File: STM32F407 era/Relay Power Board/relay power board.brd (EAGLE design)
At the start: 135.9 x 58.4 mm, 37 parts, among them X1 5566-6, X2 22-23-2031, X3 22-23-2021, X4 22-23-2021

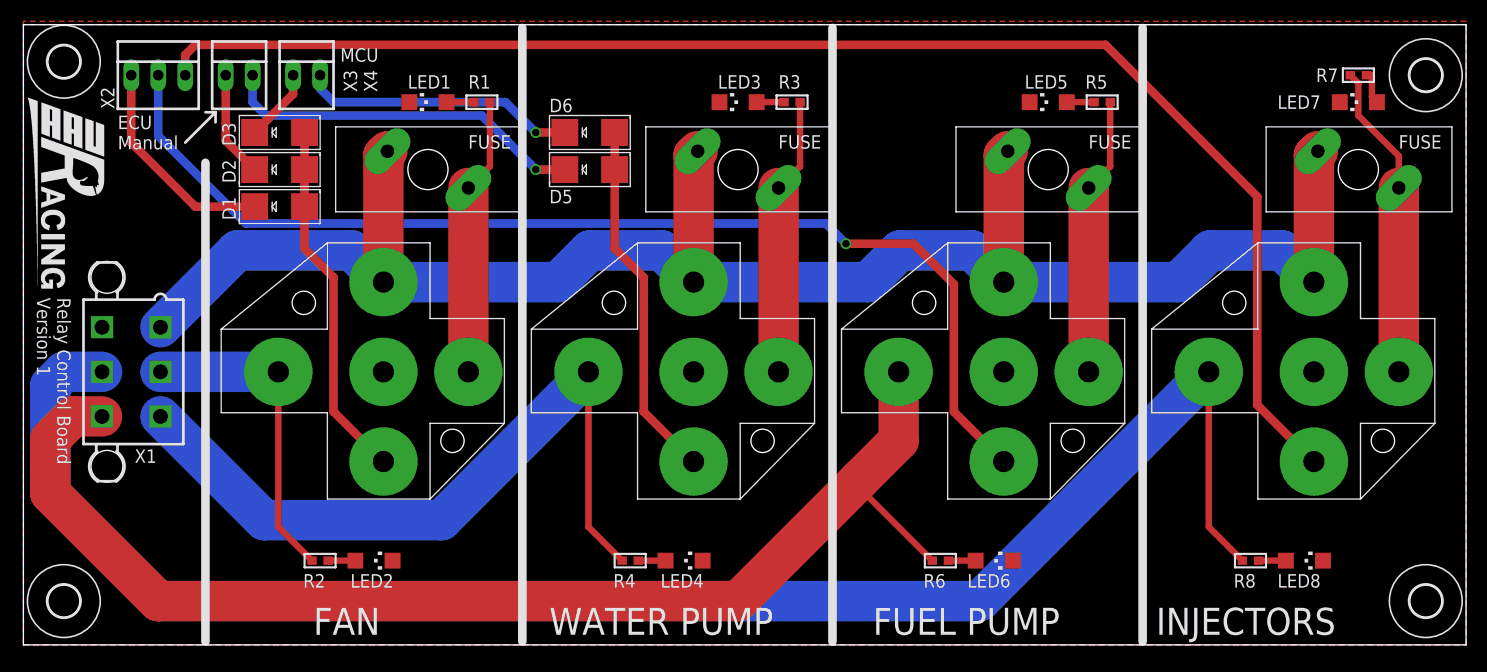
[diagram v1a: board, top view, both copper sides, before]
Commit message: silkscreen changes
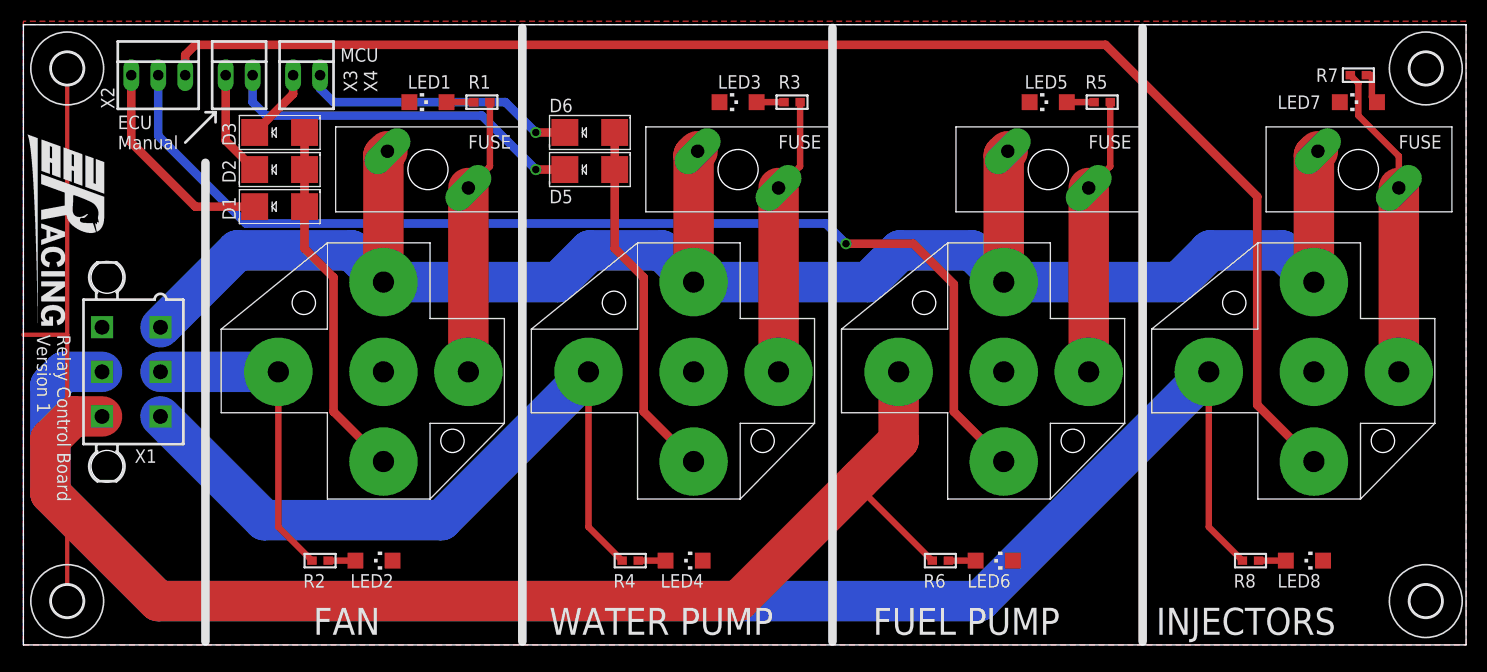
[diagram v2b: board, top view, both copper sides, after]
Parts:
- moved H3 0.71 mm to (4.13, 54.3)
- moved H2 0.63 mm to (132.1, 54.3)
- moved H6 0.32 mm to (4.13, 4.13)
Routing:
- net N$27: track 0.00 -> 54.3 mm

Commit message: All boards RC done!
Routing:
- net N$27: track 54.3 -> 0.00 mm
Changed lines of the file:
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@@
 Version 1</text>
 <wire x1="15.24" y1="47.3075" x2="18.0975" y2="50.165" width="0.254" layer="112"/>
-<dimension x1="0" y1="58.42" x2="0" y2="0" x3="-7.62" y3="29.21" layer="1"/>
-<dimension x1="135.89" y1="58.7375" x2="0" y2="58.7375" x3="67.945" y3="69.5325" layer="1"/>
-<dimension x1="0" y1="0" x2="0" y2="29.21" x3="-7.62" y3="14.605" layer="1"/>
-<dimension x1="4.1275" y1="29.21" x2="4.1275" y2="54.2925" x3="-2.2225" y3="41.75125" layer="1"/>
-<dimension x1="4.1275" y1="4.1275" x2="4.1275" y2="29.21" x3="-2.2225" y3="16.66875" layer="1"/>
-<dimension x1="0" y1="29.21" x2="4.1275" y2="29.21" x3="2.06375" y3="62.865" layer="1"/>
 <wire x1="4.1275" y1="29.21" x2="132.08" y2="29.21" width="0.4064" layer="37"/>
 <wire x1="132.08" y1="29.21" x2="132.08" y2="54.2925" width="0.4064" layer="37"/>
@@
 </signal>
 <signal name="N$27">
-<wire x1="0" y1="29.21" x2="4.1275" y2="29.21" width="0.4064" layer="1"/>
-<wire x1="4.1275" y1="29.21" x2="4.1275" y2="54.2925" width="0.4064" layer="1"/>
-<wire x1="4.1275" y1="4.1275" x2="4.1275" y2="29.21" width="0.4064" layer="1"/>
 </signal>
 </signals>
